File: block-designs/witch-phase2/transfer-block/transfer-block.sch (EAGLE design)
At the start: 20 parts, among them IC1 741G18DBVR, IC2 741G97DBVR, IC3 741G157DBVR, IC4 741G157DBVR, IC5 741G175DBVR

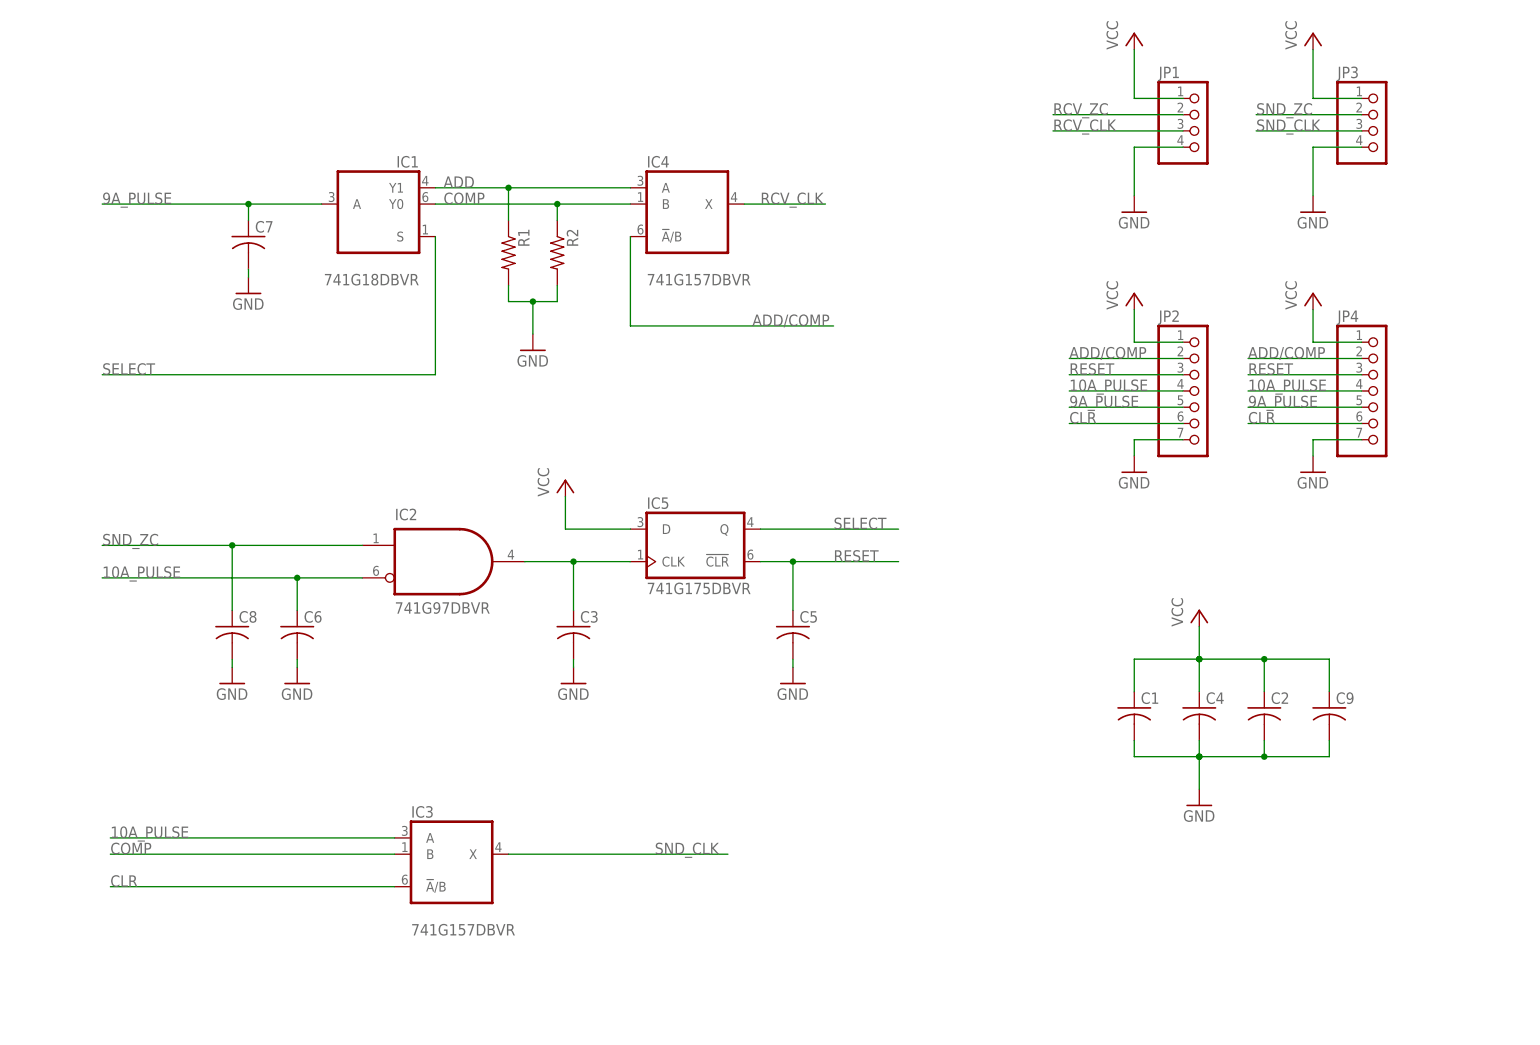
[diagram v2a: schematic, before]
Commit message: add additional logic for zero position bugs
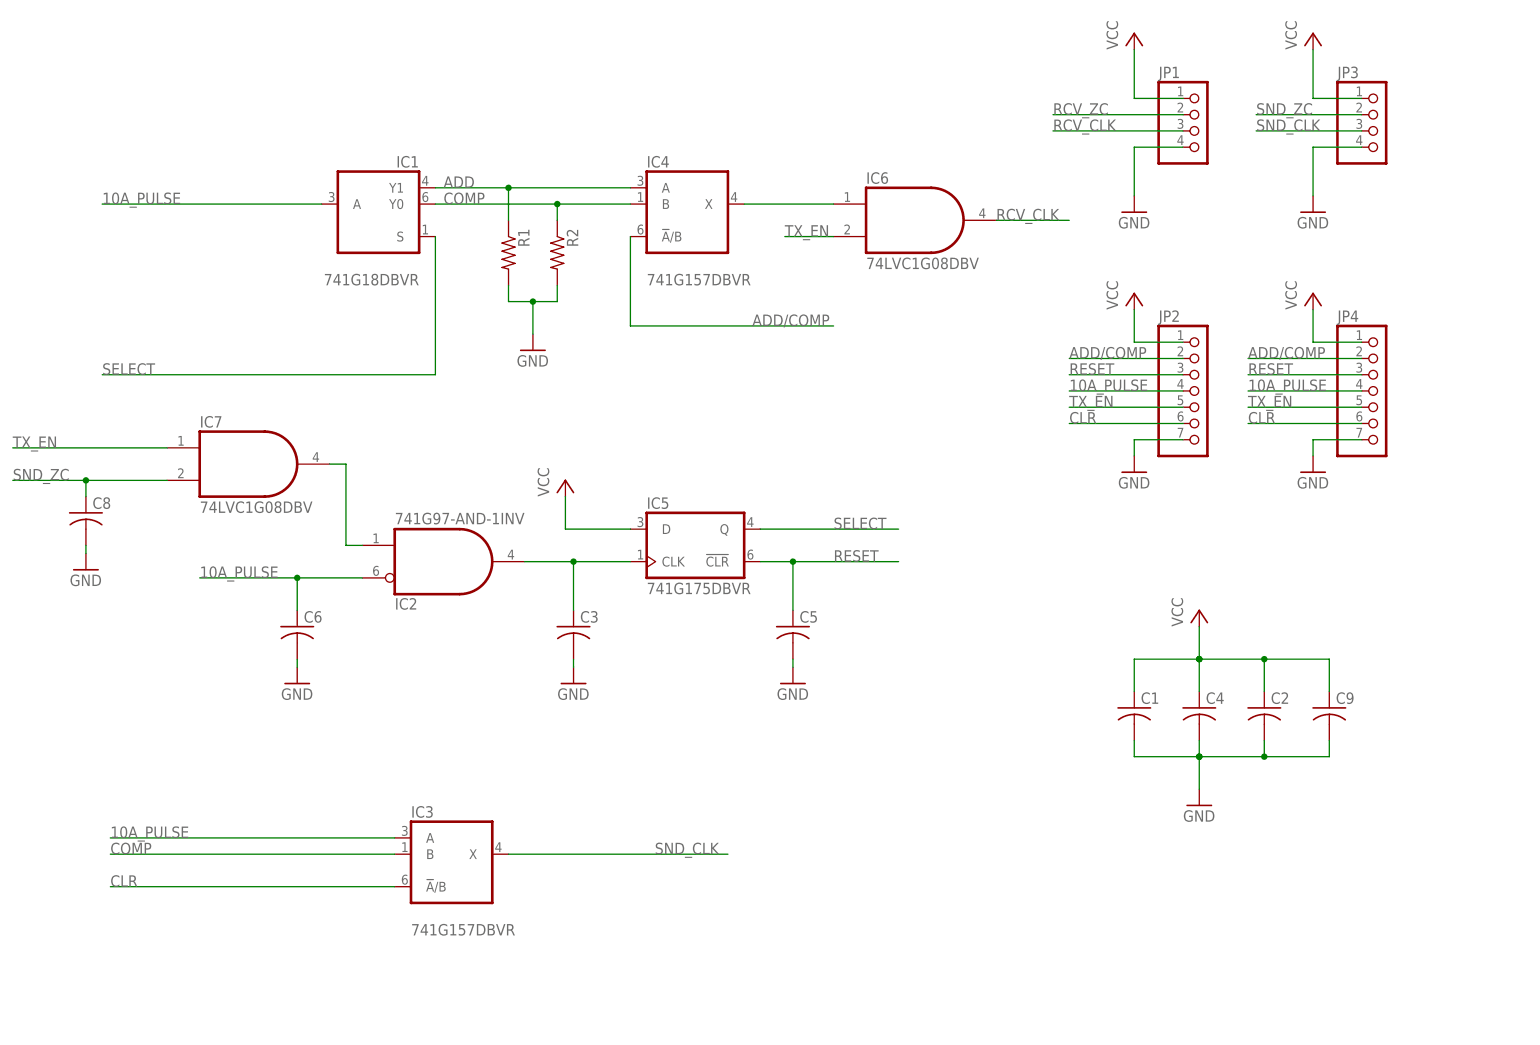
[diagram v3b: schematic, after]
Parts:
- removed C7: (no value), resistor:C-USC0603K
- added IC6, IC7: 74LVC1G08DBV, 74xx-little-us:74LVC1G08DBV
- IC2: value 741G97DBVR -> 741G97-AND-1INV
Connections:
- removed net 9A_PULSE: C7.1, IC1G$1.A, JP2.5, JP4.5
- new net N$1: IC2A.I1, IC7A.O
- new net PRE_RCV_CLK: IC4G$1.X, IC6A.I0
- new net TX_EN: IC6A.I1, IC7A.I0, JP2.5, JP4.5
- net 10A_PULSE: now also IC1G$1.A, IC2A.I0; no longer IC2G$1.I0
- net GND: no longer C7.2
- net RCV_CLK: now also IC6A.O; no longer IC4G$1.X
- net SND_ZC: now also IC7A.I1; no longer IC2G$1.I1
- net ZC_EN: now also IC2A.O; no longer IC2G$1.O
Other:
- moved on the sheet: C8
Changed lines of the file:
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@@
 <part name="C6" library="resistor" deviceset="C-US" device="C0603K"/>
 <part name="GND9" library="supply1" deviceset="GND" device=""/>
-<part name="C7" library="resistor" deviceset="C-US" device="C0603K"/>
-<part name="GND10" library="supply1" deviceset="GND" device=""/>
 <part name="C8" library="resistor" deviceset="C-US" device="C0603K"/>
 <part name="GND11" library="supply1" deviceset="GND" device=""/>
-<part name="IC2" library="witch-e" deviceset="74*1G97-AND-1INV" device="" value="741G97DBVR"/>
 <part name="C9" library="resistor" deviceset="C-US" device="C0603K"/>
+<part name="IC6" library="74xx-little-us" deviceset="74*1G08" device="DBV" technology="LVC"/>
+<part name="IC7" library="74xx-little-us" deviceset="74*1G08" device="DBV" technology="LVC"/>
+<part name="IC2" library="witch-e" deviceset="74*1G97-AND-1INV" device=""/>
 </parts>
 <sheets>
@@
 <instance part="C6" gate="G$1" x="48.26" y="83.82"/>
 <instance part="GND9" gate="1" x="48.26" y="74.93"/>
-<instance part="C7" gate="G$1" x="40.64" y="144.78"/>
-<instance part="GND10" gate="1" x="40.64" y="135.89"/>
-<instance part="C8" gate="G$1" x="38.1" y="83.82"/>
-<instance part="GND11" gate="1" x="38.1" y="74.93"/>
-<instance part="IC2" gate="G$1" x="71.12" y="93.98" smashed="yes" rot="MR180">
-<attribute name="NAME" x="63.5" y="102.235" size="1.778" layer="95" rot="MR180"/>
-<attribute name="VALUE" x="63.5" y="87.63" size="1.778" layer="96" rot="MR180"/>
-</instance>
+<instance part="C8" gate="G$1" x="15.24" y="101.6"/>
+<instance part="GND11" gate="1" x="15.24" y="92.71"/>
 <instance part="C9" gate="G$1" x="209.55" y="71.12"/>
+<instance part="IC6" gate="A" x="144.78" y="147.32"/>
+<instance part="IC7" gate="A" x="40.64" y="109.22"/>
+<instance part="IC2" gate="A" x="71.12" y="93.98" rot="MR180"/>
 </instances>
 <busses>
@@
 </segment>
 <segment>
-<pinref part="GND10" gate="1" pin="GND"/>
-<pinref part="C7" gate="G$1" pin="2"/>
-<wire x1="40.64" y1="138.43" x2="40.64" y2="139.7" width="0.1524" layer="91"/>
-</segment>
-<segment>
 <pinref part="GND11" gate="1" pin="GND"/>
 <pinref part="C8" gate="G$1" pin="2"/>
-<wire x1="38.1" y1="77.47" x2="38.1" y2="78.74" width="0.1524" layer="91"/>
+<wire x1="15.24" y1="95.25" x2="15.24" y2="96.52" width="0.1524" layer="91"/>
 </segment>
 </net>
@@
 </segment>
 <segment>
-<label x="17.78" y="91.44" size="1.778" layer="95"/>
+<label x="33.02" y="91.44" size="1.778" layer="95"/>
 <wire x1="58.42" y1="91.44" x2="48.26" y2="91.44" width="0.1524" layer="91"/>
 <pinref part="C6" gate="G$1" pin="1"/>
-<wire x1="48.26" y1="91.44" x2="17.78" y2="91.44" width="0.1524" layer="91"/>
+<wire x1="48.26" y1="91.44" x2="33.02" y2="91.44" width="0.1524" layer="91"/>
 <wire x1="48.26" y1="86.36" x2="48.26" y2="91.44" width="0.1524" layer="91"/>
 <junction x="48.26" y="91.44"/>
-<pinref part="IC2" gate="G$1" pin="I0"/>
+<pinref part="IC2" gate="A" pin="I0"/>
+</segment>
+<segment>
+<pinref part="IC1" gate="G$1" pin="A"/>
+<wire x1="17.78" y1="149.86" x2="52.07" y2="149.86" width="0.1524" layer="91"/>
+<label x="17.78" y="149.86" size="1.778" layer="95"/>
 </segment>
 </net>
 <net name="SND_ZC" class="0">
 <segment>
-<wire x1="58.42" y1="96.52" x2="38.1" y2="96.52" width="0.1524" layer="91"/>
-<label x="17.78" y="96.52" size="1.778" layer="95"/>
+<label x="3.81" y="106.68" size="1.778" layer="95"/>
 <pinref part="C8" gate="G$1" pin="1"/>
-<wire x1="38.1" y1="96.52" x2="17.78" y2="96.52" width="0.1524" layer="91"/>
-<wire x1="38.1" y1="96.52" x2="38.1" y2="86.36" width="0.1524" layer="91"/>
-<junction x="38.1" y="96.52"/>
-<pinref part="IC2" gate="G$1" pin="I1"/>
+<wire x1="15.24" y1="106.68" x2="3.81" y2="106.68" width="0.1524" layer="91"/>
+<wire x1="15.24" y1="106.68" x2="15.24" y2="104.14" width="0.1524" layer="91"/>
+<pinref part="IC7" gate="A" pin="I1"/>
+<wire x1="27.94" y1="106.68" x2="15.24" y2="106.68" width="0.1524" layer="91"/>
+<junction x="15.24" y="106.68"/>
 </segment>
 <segment>
@@
 <wire x1="91.44" y1="86.36" x2="91.44" y2="93.98" width="0.1524" layer="91"/>
 <junction x="91.44" y="93.98"/>
-<pinref part="IC2" gate="G$1" pin="O"/>
+<pinref part="IC2" gate="A" pin="O"/>
 </segment>
 </net>
@@
 </segment>
 <segment>
-<pinref part="IC4" gate="G$1" pin="X"/>
-<wire x1="118.11" y1="149.86" x2="130.81" y2="149.86" width="0.1524" layer="91"/>
-<label x="120.65" y="149.86" size="1.778" layer="95"/>
-</segment>
-</net>
-<net name="9A_PULSE" class="0">
-<segment>
-<pinref part="JP4" gate="A" pin="5"/>
-<wire x1="214.63" y1="118.11" x2="196.85" y2="118.11" width="0.1524" layer="91"/>
-<label x="196.85" y="118.11" size="1.778" layer="95"/>
-</segment>
-<segment>
-<pinref part="JP2" gate="A" pin="5"/>
-<wire x1="186.69" y1="118.11" x2="168.91" y2="118.11" width="0.1524" layer="91"/>
-<label x="168.91" y="118.11" size="1.778" layer="95"/>
-</segment>
-<segment>
-<pinref part="IC1" gate="G$1" pin="A"/>
-<wire x1="17.78" y1="149.86" x2="40.64" y2="149.86" width="0.1524" layer="91"/>
-<label x="17.78" y="149.86" size="1.778" layer="95"/>
-<pinref part="C7" gate="G$1" pin="1"/>
-<wire x1="40.64" y1="149.86" x2="52.07" y2="149.86" width="0.1524" layer="91"/>
-<wire x1="40.64" y1="147.32" x2="40.64" y2="149.86" width="0.1524" layer="91"/>
-<junction x="40.64" y="149.86"/>
+<pinref part="IC6" gate="A" pin="O"/>
+<wire x1="157.48" y1="147.32" x2="168.91" y2="147.32" width="0.1524" layer="91"/>
+<label x="157.48" y="147.32" size="1.778" layer="95"/>
 </segment>
 </net>
@@
 </segment>
 </net>
+<net name="TX_EN" class="0">
+<segment>
+<pinref part="IC7" gate="A" pin="I0"/>
+<wire x1="27.94" y1="111.76" x2="3.81" y2="111.76" width="0.1524" layer="91"/>
+<label x="3.81" y="111.76" size="1.778" layer="95"/>
+</segment>
+<segment>
+<pinref part="IC6" gate="A" pin="I1"/>
+<wire x1="132.08" y1="144.78" x2="124.46" y2="144.78" width="0.1524" layer="91"/>
+<label x="124.46" y="144.78" size="1.778" layer="95"/>
+</segment>
+<segment>
+<pinref part="JP4" gate="A" pin="5"/>
+<wire x1="214.63" y1="118.11" x2="196.85" y2="118.11" width="0.1524" layer="91"/>
+<label x="196.85" y="118.11" size="1.778" layer="95"/>
+</segment>
+<segment>
+<pinref part="JP2" gate="A" pin="5"/>
+<wire x1="186.69" y1="118.11" x2="168.91" y2="118.11" width="0.1524" layer="91"/>
+<label x="168.91" y="118.11" size="1.778" layer="95"/>
+</segment>
+</net>
+<net name="PRE_RCV_CLK" class="0">
+<segment>
+<pinref part="IC4" gate="G$1" pin="X"/>
+<wire x1="118.11" y1="149.86" x2="132.08" y2="149.86" width="0.1524" layer="91"/>
+<pinref part="IC6" gate="A" pin="I0"/>
+</segment>
+</net>
+<net name="N$1" class="0">
+<segment>
+<pinref part="IC7" gate="A" pin="O"/>
+<wire x1="53.34" y1="109.22" x2="55.88" y2="109.22" width="0.1524" layer="91"/>
+<wire x1="55.88" y1="109.22" x2="55.88" y2="96.52" width="0.1524" layer="91"/>
+<wire x1="55.88" y1="96.52" x2="58.42" y2="96.52" width="0.1524" layer="91"/>
+<pinref part="IC2" gate="A" pin="I1"/>
+</segment>
+</net>

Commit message: add component values and manufacturing information
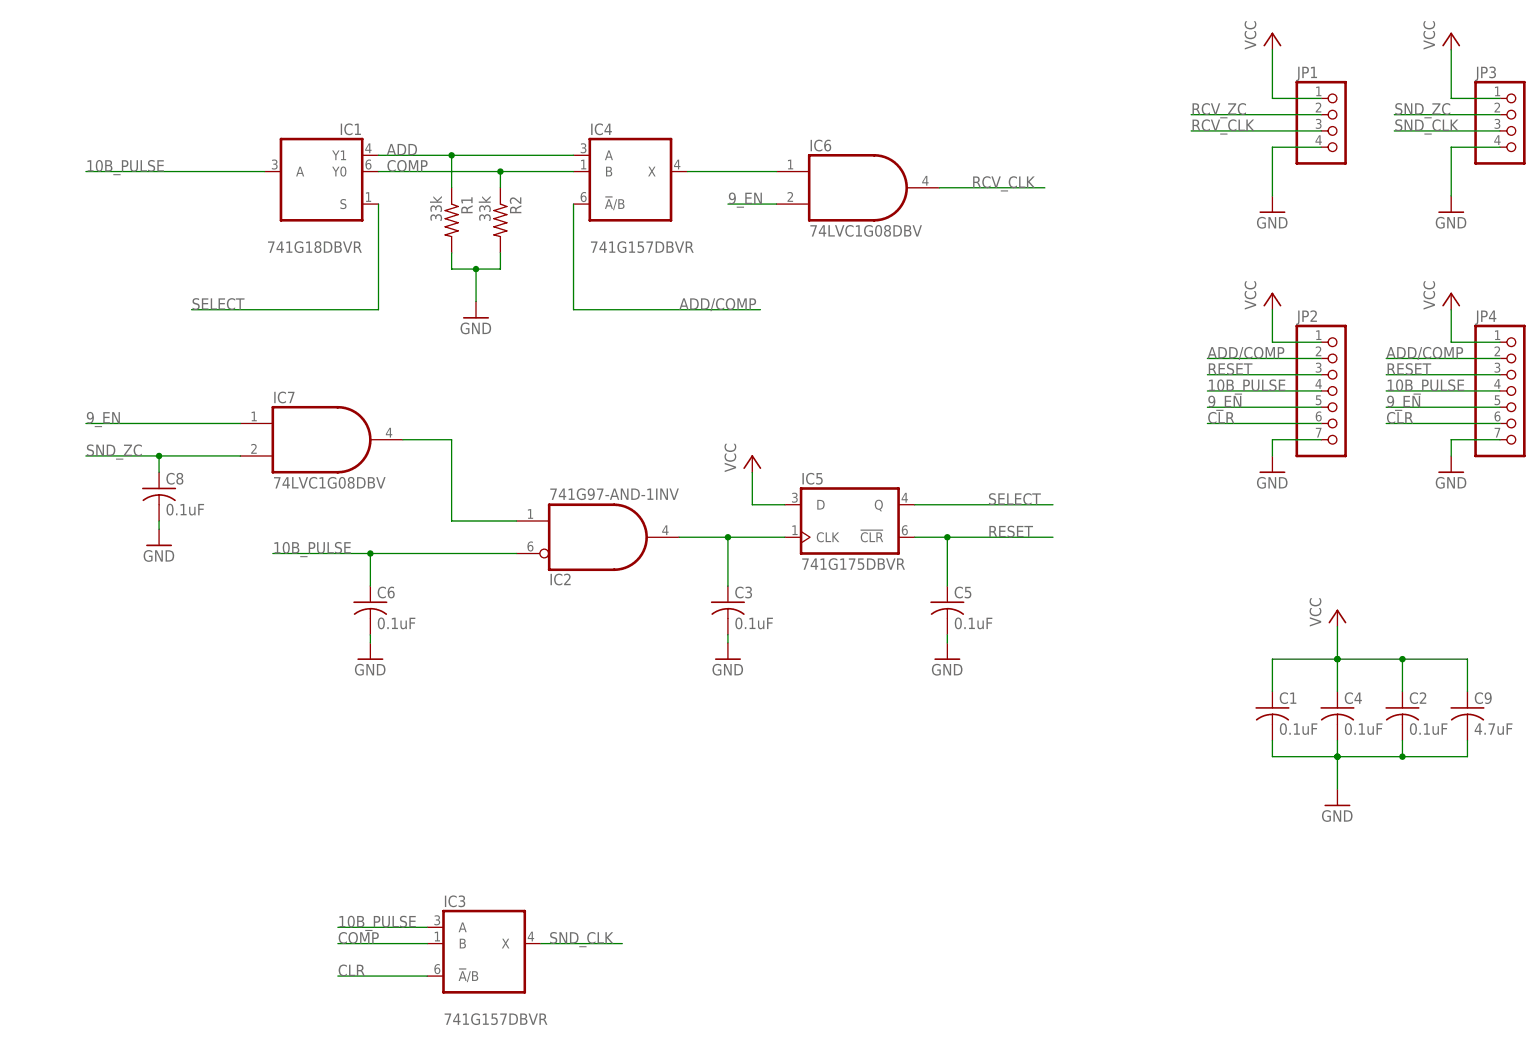
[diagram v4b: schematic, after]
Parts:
- C1, C2, C3, C4, C5, C6, C8: value (none) -> 0.1uF
- C9: value (none) -> 4.7uF
- R1, R2: value (none) -> 33k
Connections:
- net 10A_PULSE renamed 10B_PULSE
- net TX_EN renamed 9_EN
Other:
- moved on the sheet: C1, C2, C3, C4, C5, C6, C8, C9, IC1, IC2, IC3, IC4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
